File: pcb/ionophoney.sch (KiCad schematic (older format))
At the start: 0 parts

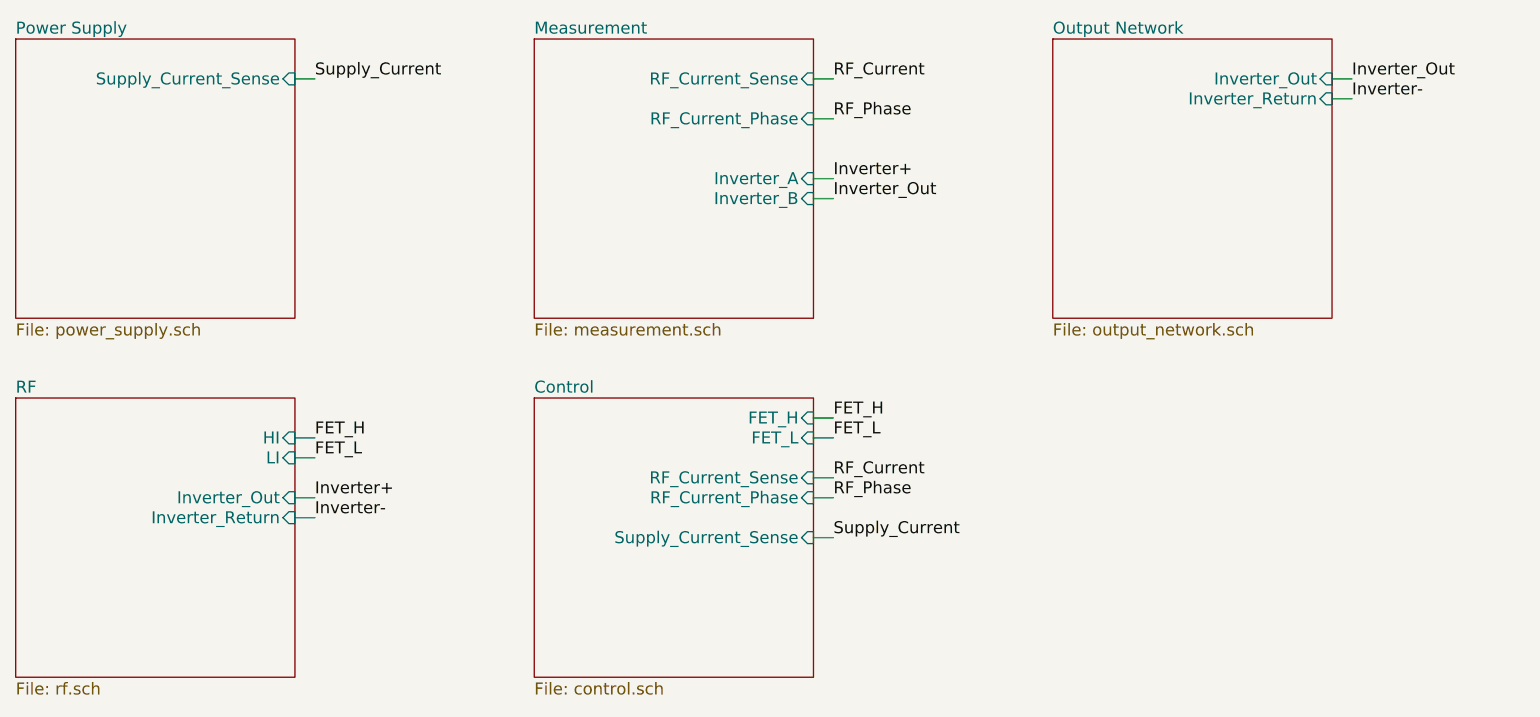
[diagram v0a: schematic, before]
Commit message: added measurements and simulation
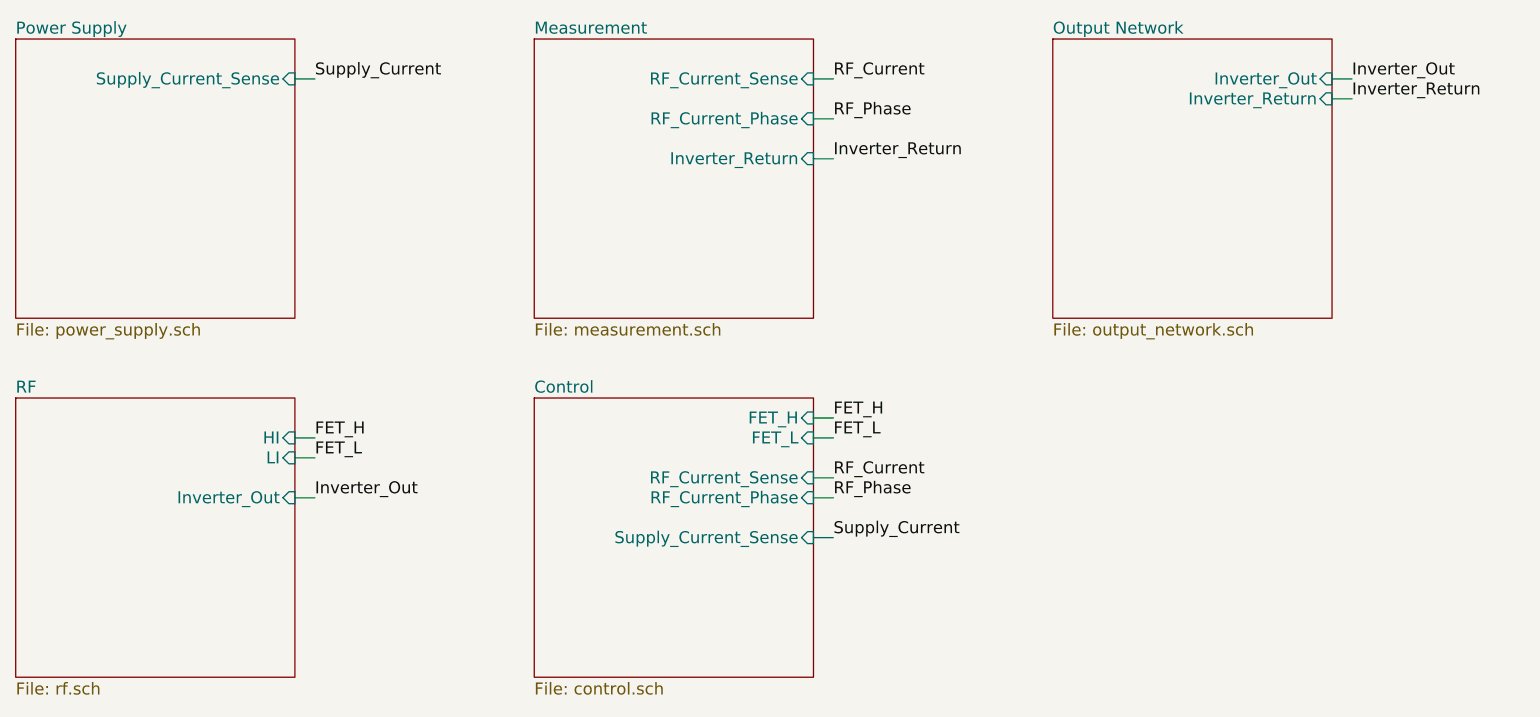
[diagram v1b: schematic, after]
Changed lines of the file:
@@
 F3 "LI" I R 2600 3400 60
 F4 "Inverter_Out" I R 2600 3600 60
-F5 "Inverter_Return" I R 2600 3700 60
 $EndSheet
 $Sheet
@@
 F2 "RF_Current_Sense" I R 5200 1500 60
 F3 "RF_Current_Phase" I R 5200 1700 60
-F4 "Inverter_A" I R 5200 2000 60
-F5 "Inverter_B" I R 5200 2100 60
+F4 "Inverter_Return" I R 5200 1900 60
 $EndSheet
 $Sheet
@@
 	2600 3600 2700 3600
 Wire Wire Line
-	2600 3700 2700 3700
-Wire Wire Line
 	2600 1500 2700 1500
 Wire Wire Line
@@
 Wire Wire Line
 	5200 1700 5300 1700
-Wire Wire Line
-	5200 2000 5300 2000
-Wire Wire Line
-	5200 2100 5300 2100
 Wire Wire Line
 	5200 3200 5300 3200
@@
 Supply_Current
 Text Label 2700 3600 0    60   ~ 0
-Inverter+
-Text Label 2700 3700 0    60   ~ 0
-Inverter-
-Text Label 5300 2000 0    60   ~ 0
-Inverter+
-Text Label 5300 2100 0    60   ~ 0
 Inverter_Out
 Text Label 7900 1500 0    60   ~ 0
 Inverter_Out
 Text Label 7900 1600 0    60   ~ 0
-Inverter-
+Inverter_Return
+Wire Wire Line
+	5200 1900 5300 1900
+Text Label 5300 1900 0    60   ~ 0
+Inverter_Return
 $EndSCHEMATC

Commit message: new GaN test board
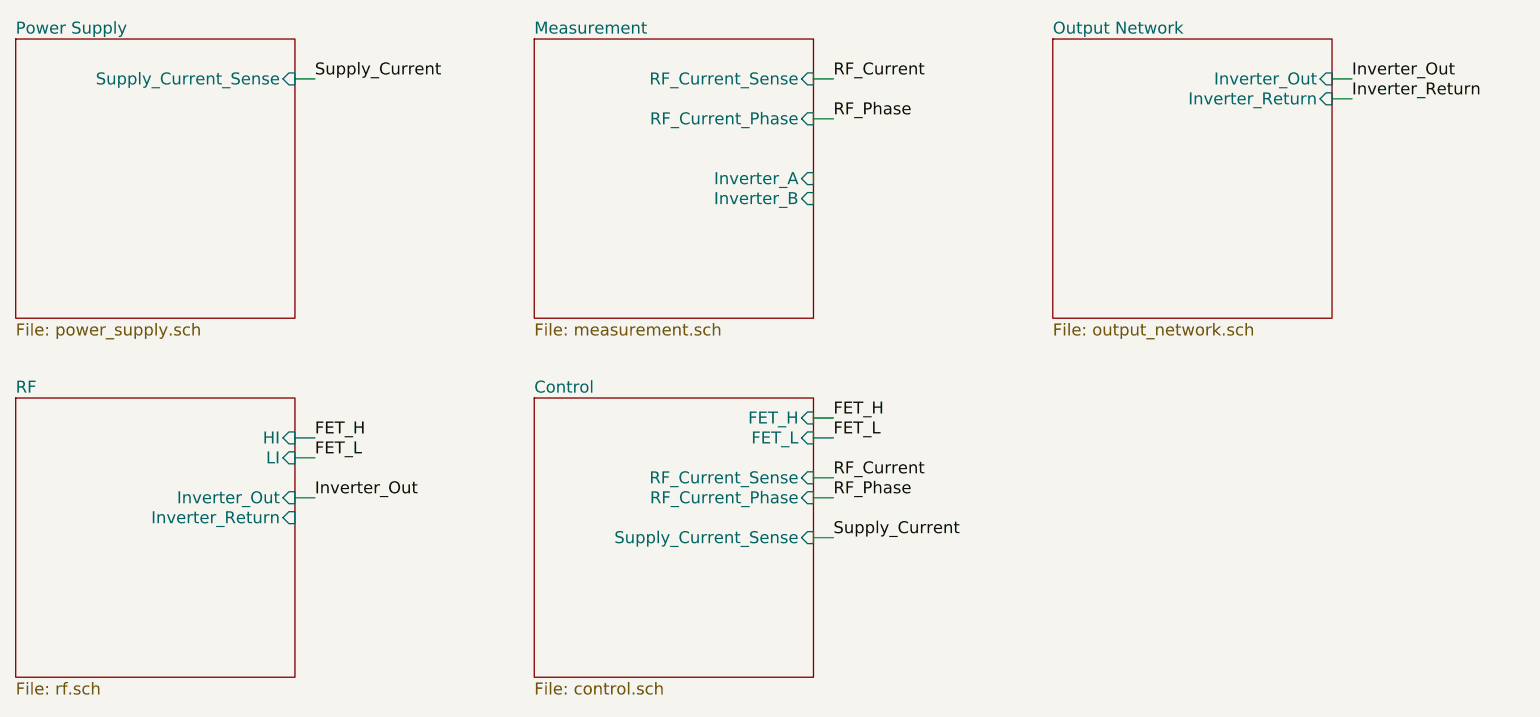
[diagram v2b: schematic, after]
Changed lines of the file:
@@
 LIBS:valves
 LIBS:wbraun_ic_lib
+LIBS:ionophoney-cache
 EELAYER 25 0
 EELAYER END
@@
 $EndSheet
 $Sheet
-S 1200 3100 1400 1400
-U 5703397E
-F0 "RF" 60
-F1 "rf.sch" 60
-F2 "HI" I R 2600 3300 60
-F3 "LI" I R 2600 3400 60
-F4 "Inverter_Out" I R 2600 3600 60
-$EndSheet
-$Sheet
 S 3800 3100 1400 1400
 U 57033981
@@
 F2 "RF_Current_Sense" I R 5200 1500 60
 F3 "RF_Current_Phase" I R 5200 1700 60
-F4 "Inverter_Return" I R 5200 1900 60
+F4 "Inverter_A" I R 5200 2000 60
+F5 "Inverter_B" I R 5200 2100 60
 $EndSheet
 $Sheet
@@
 Text Label 7900 1600 0    60   ~ 0
 Inverter_Return
-Wire Wire Line
-	5200 1900 5300 1900
-Text Label 5300 1900 0    60   ~ 0
-Inverter_Return
+$Sheet
+S 1200 3100 1400 1400
+U 5703397E
+F0 "RF" 60
+F1 "rf.sch" 60
+F2 "HI" I R 2600 3300 60
+F3 "LI" I R 2600 3400 60
+F4 "Inverter_Out" I R 2600 3600 60
+F5 "Inverter_Return" I R 2600 3700 60
+$EndSheet
 $EndSCHEMATC
